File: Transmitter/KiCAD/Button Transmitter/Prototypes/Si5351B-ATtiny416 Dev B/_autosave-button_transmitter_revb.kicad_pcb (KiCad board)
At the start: 2 copper layers, 25 x 25 mm, 4 parts, among them J1 Antenna Screw Pad

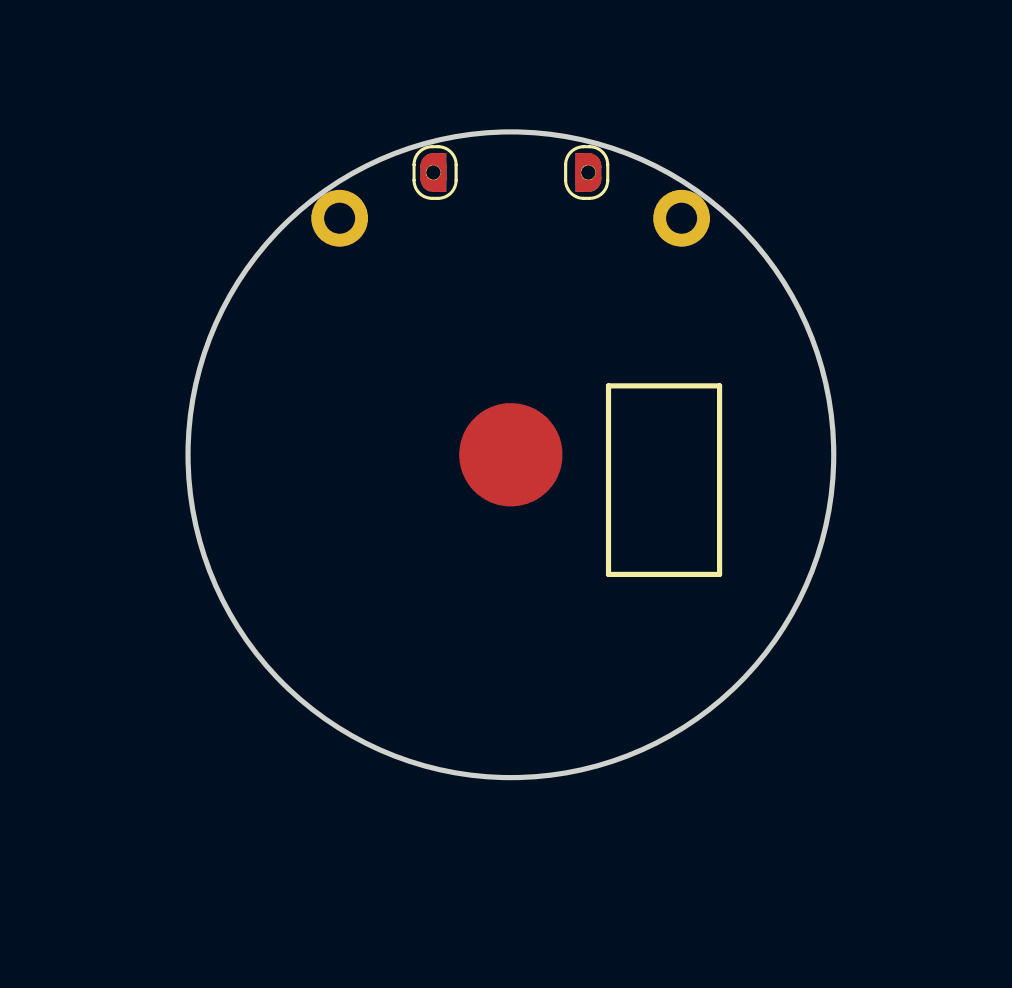
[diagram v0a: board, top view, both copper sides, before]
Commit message: More Dev B schematic tweaks
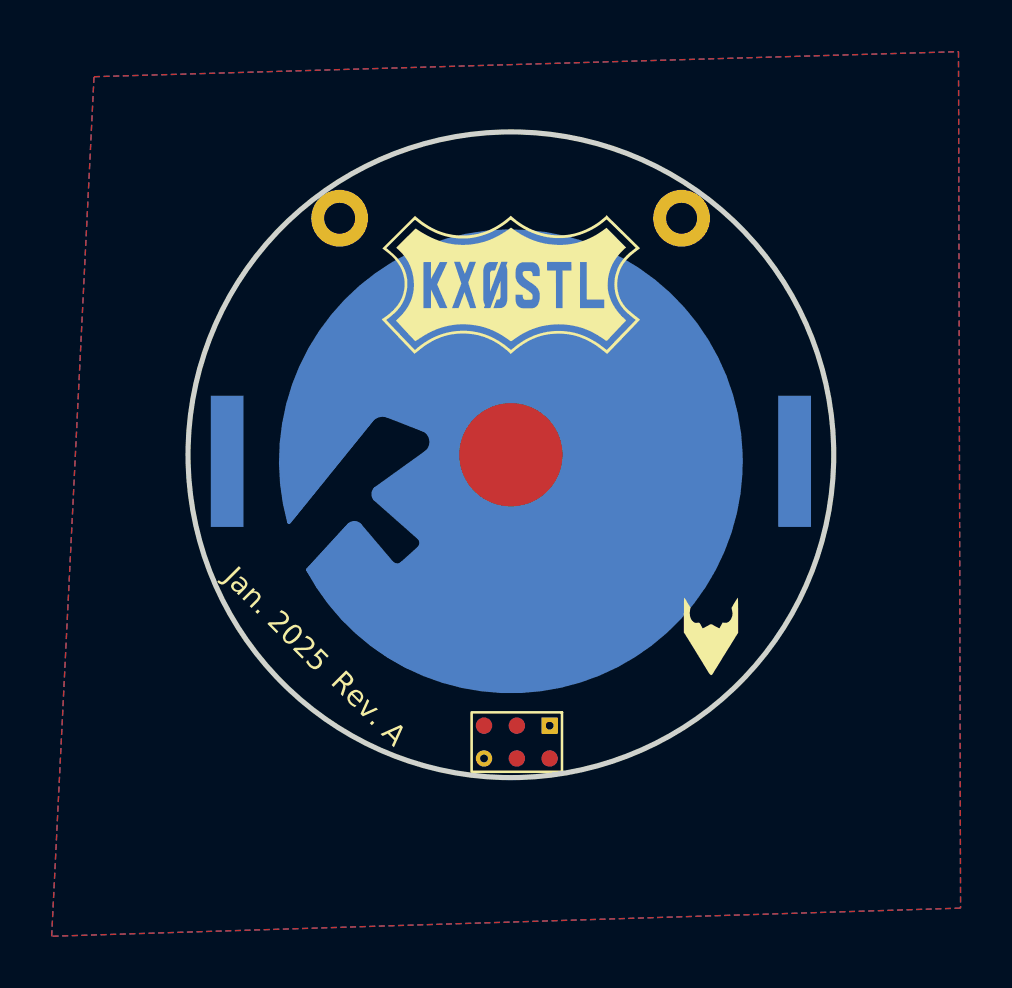
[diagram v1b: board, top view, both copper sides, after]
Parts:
- removed BZ1: 7BB-20-3, Library:Buzzer_Pad_POS
- removed BZ2-1: 7BB-20-3, Library:Buzzer_Pad_NEG
- added BT1: CR2032, Library:BatteryHolder_Keystone_3034_1x20mm_CUTOUT, B.Cu at (75.6, 104.2)
- added G***: LOGO, Library:Logo_10mm_inv, F.Cu at (75.6, 97.3)
- added G***: LOGO, Library:IPL_Logo_3mm, F.Cu at (83.4, 111.0)
- added J2: 1.27mm Pogo Pads For Programming & Debug, Library:2x3_1.27mm_Pogo_Header, F.Cu at (75.8, 115.0)
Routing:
- added copper zone on B.Cu, net GND
- added copper zone on F.Cu, net GND
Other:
- board text added: "Jan. 2025"
- board text added: "Rev. A"
